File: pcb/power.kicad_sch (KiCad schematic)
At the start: 7 parts

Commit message: Changed resistor and cap footprints to CRGM
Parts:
- R12: footprint Resistor_SMD:R_0603_1608Metric -> CRGM Passive:R_0603_1608Metric
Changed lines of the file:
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@@
 			)
 		)
-		(property "Footprint" "Resistor_SMD:R_0603_1608Metric"
+		(property "Footprint" "CRGM Passive:R_0603_1608Metric"
 			(at 45.72 36.83 0)
 			(effects

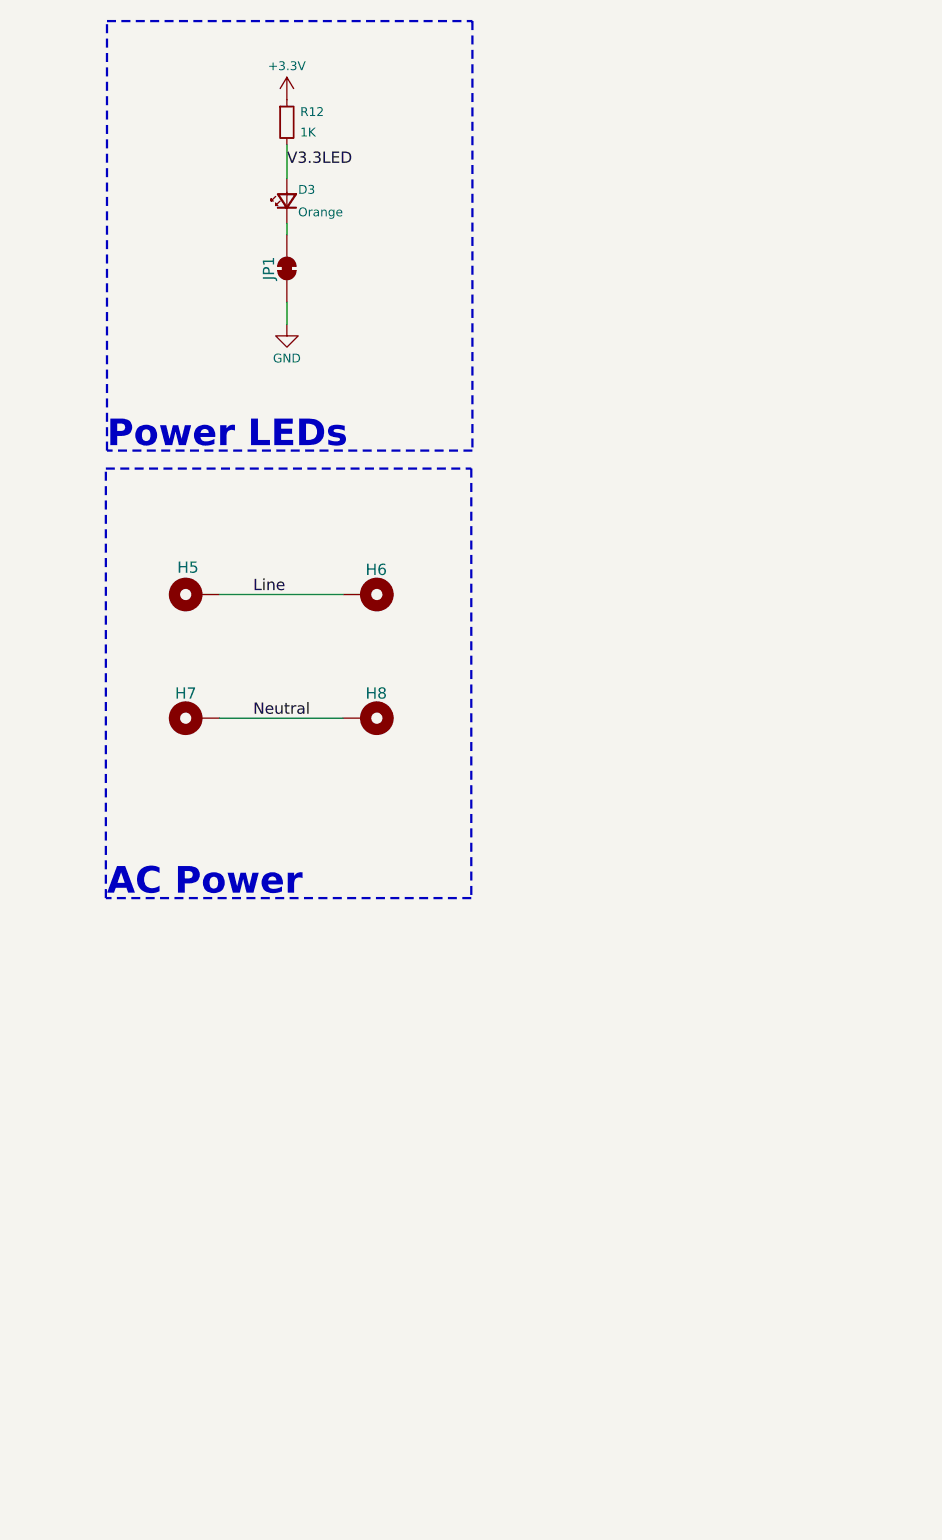
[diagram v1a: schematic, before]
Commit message: Removed CSV bom file; moved logos to symbols
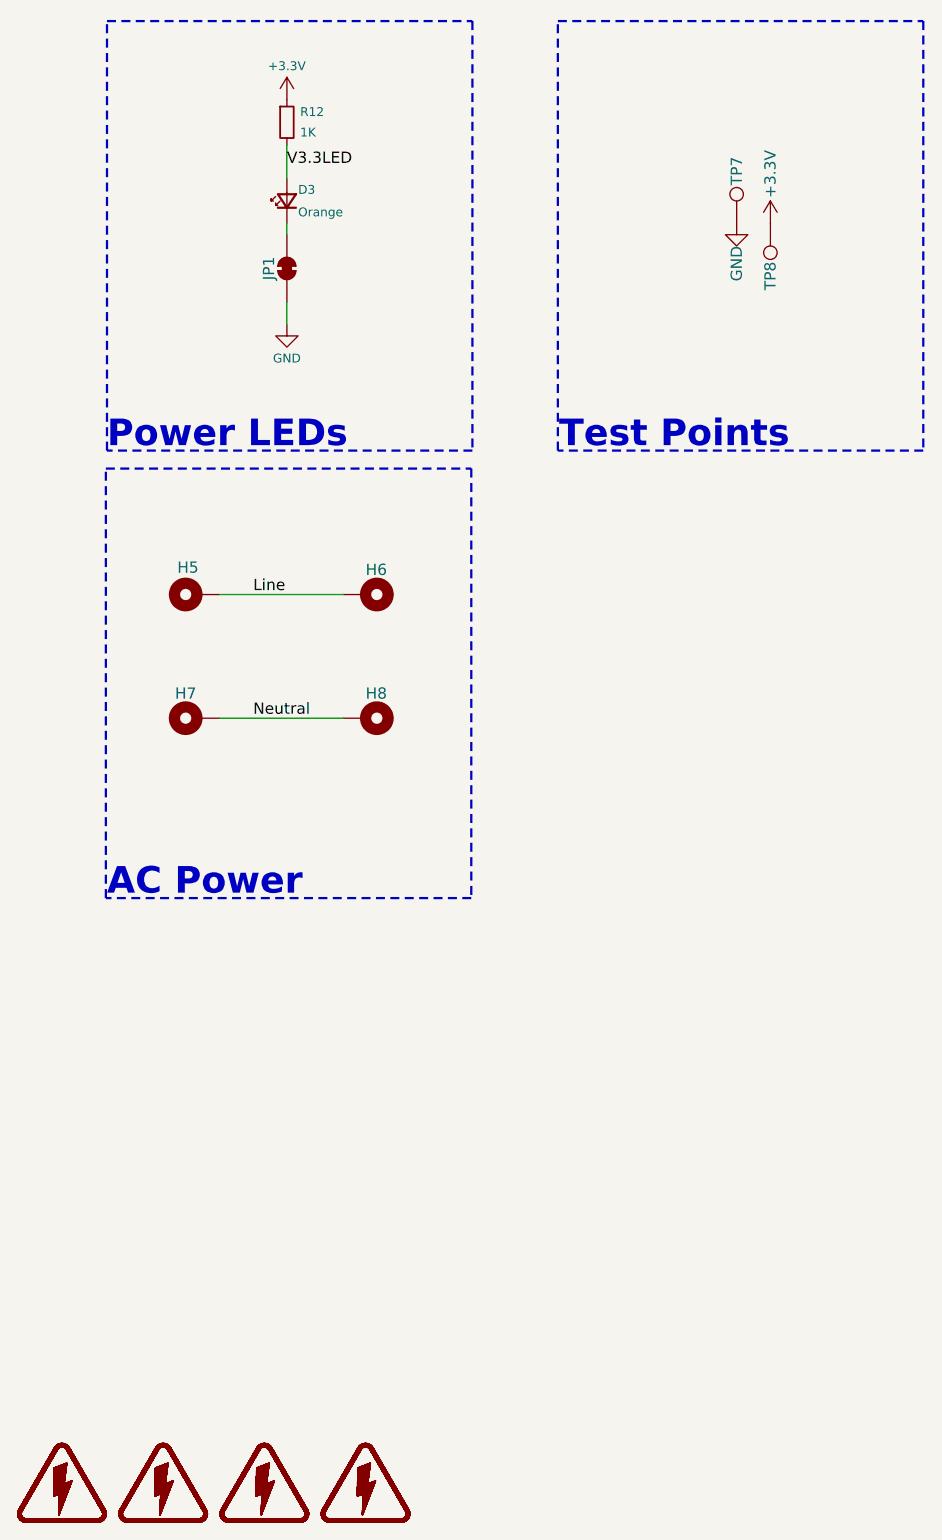
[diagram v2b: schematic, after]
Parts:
- added S1, S2, S3, S4: ~, CRGM Symbols:HIGH-VOLTAGE-5MM, symbol CRGM Symbols:High Voltage
- added TP7, TP8: ~, CRGM Mechanical:TestPoint_Pad_D1.0mm, symbol Connector:TestPoint
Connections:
- net +3.3V: now also TP8.1
- net GND: now also TP7.1
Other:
- note added: "Test Points"
- title: Current Detector -> Current Sensor

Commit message: Updated to all CRGM footprints
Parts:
- D3: footprint LED_SMD:LED_0603_1608Metric -> CRG Makes:LED_0603_1608Metric
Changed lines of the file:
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@@
 			)
 		)
-		(property "Footprint" "LED_SMD:LED_0603_1608Metric"
+		(property "Footprint" "CRG Makes:LED_0603_1608Metric"
 			(at 45.72 45.72 0)
 			(effects

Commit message: Updated part properties for consistency
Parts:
- R12: MN Vishay -> FOJAN; MPN CRCW06031K00FKEA -> FRC0603J102 TS; Tolerance (none) -> 5%
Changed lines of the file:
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@@
 			)
 		)
-		(property "MN" "Vishay"
+		(property "MN" "FOJAN"
 			(at 45.72 36.83 0)
 			(effects
@@
 			)
 		)
-		(property "MPN" "CRCW06031K00FKEA"
+		(property "MPN" "FRC0603J102 TS"
 			(at 45.72 36.83 0)
 			(effects
@@
 				)
 				(hide yes)
+			)
+		)
+		(property "Tolerance" "5%"
+			(at 45.72 36.83 0)
+			(effects
+				(font
+					(size 1.27 1.27)
+				)
+				(hide yes)

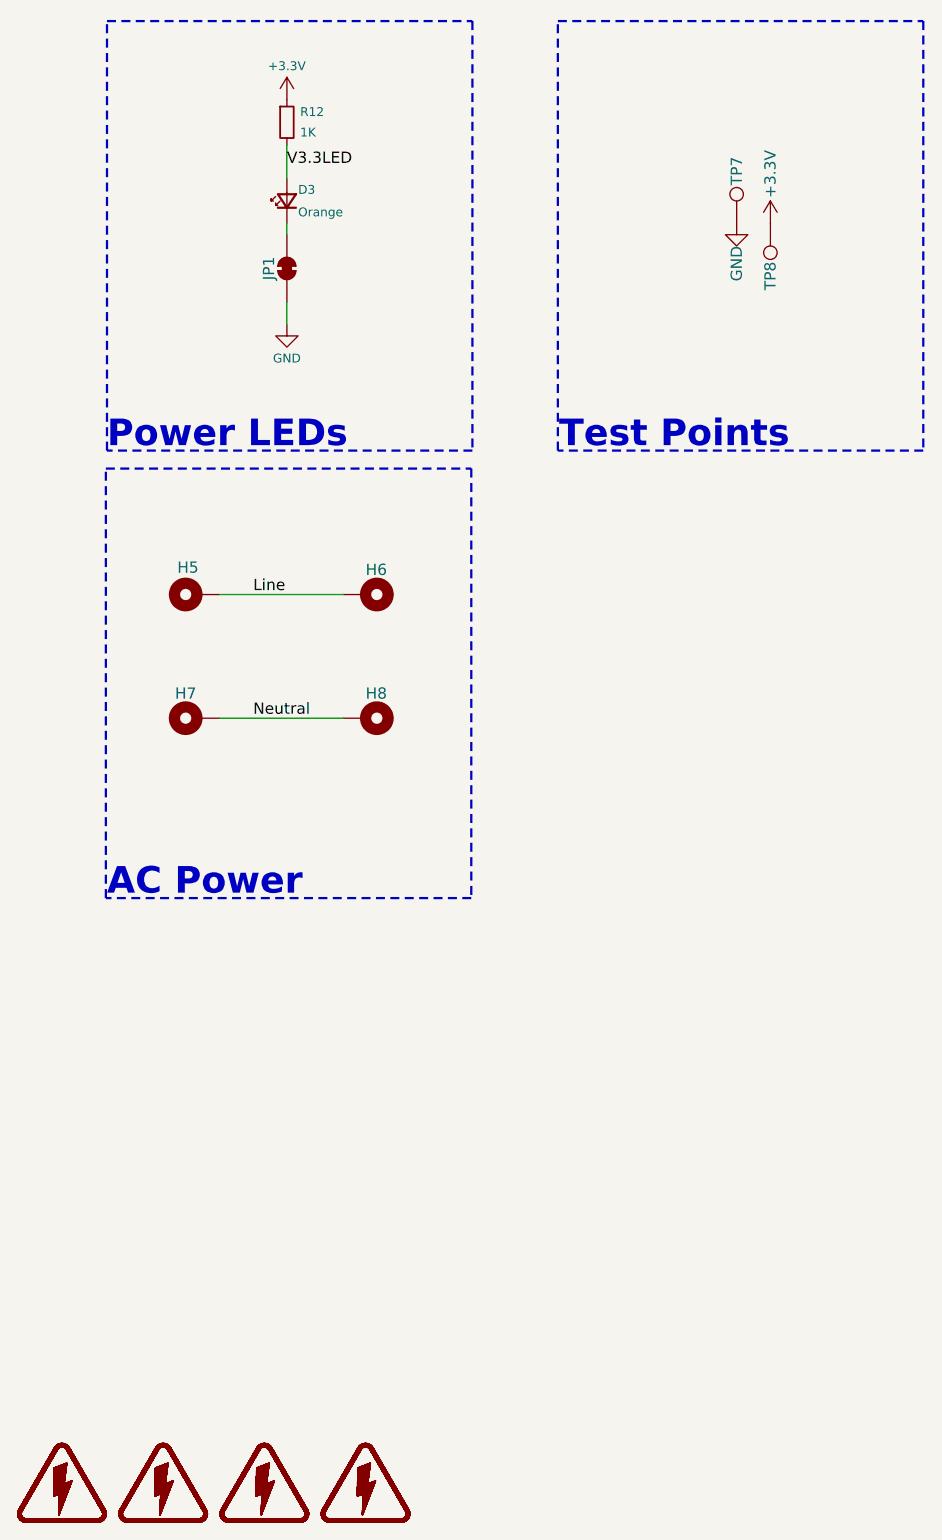
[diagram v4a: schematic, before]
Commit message: Fixed line thickness
Moved logos
Fixed board fillet to 3mm
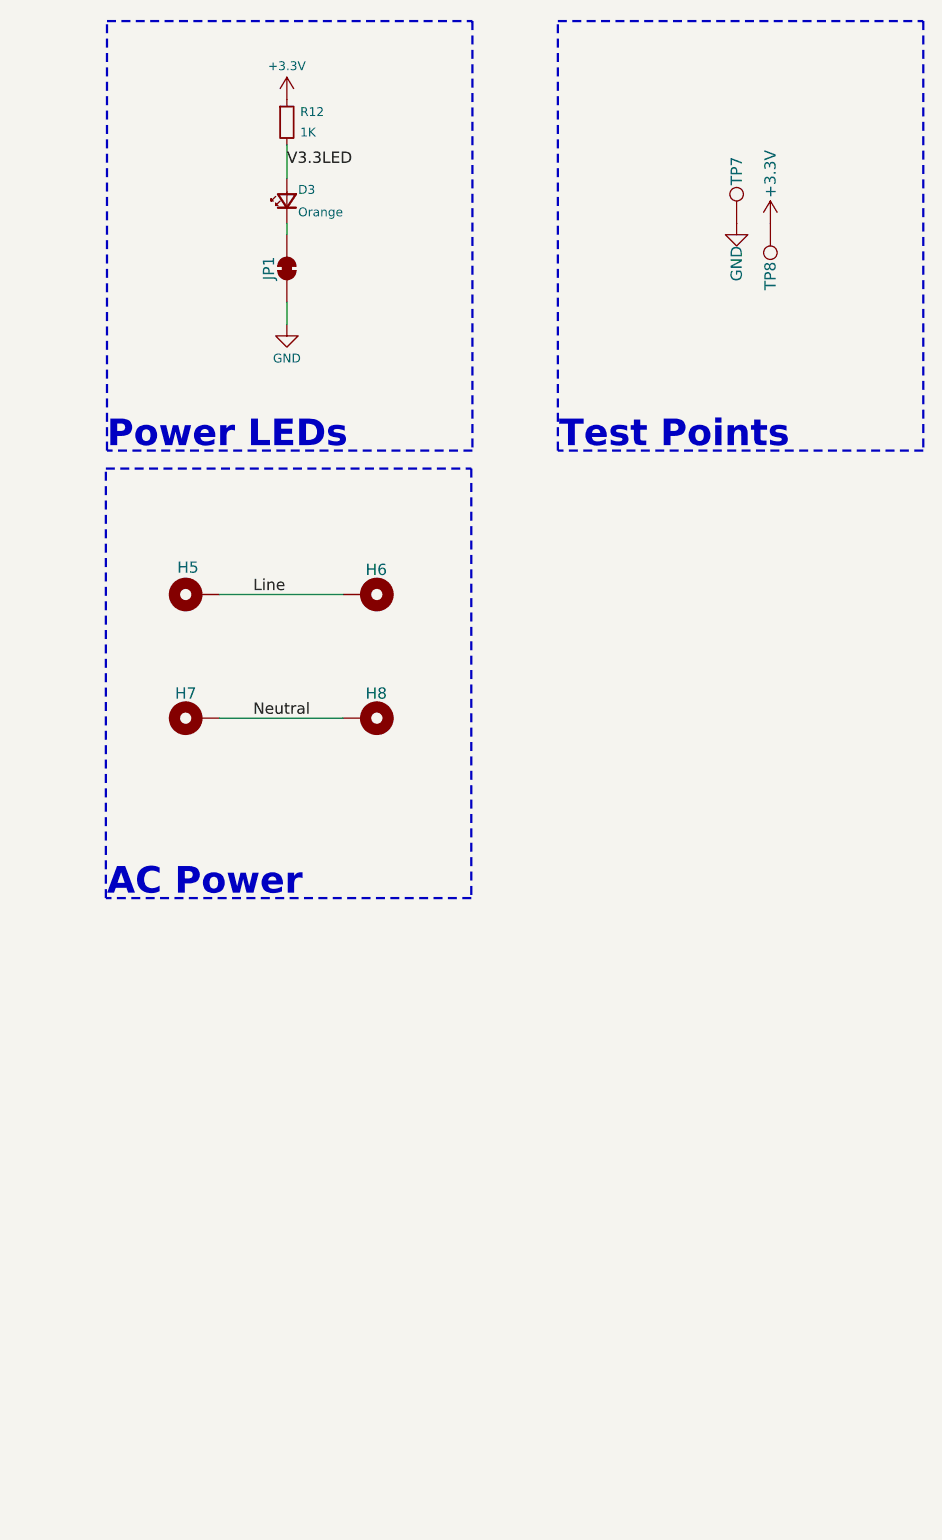
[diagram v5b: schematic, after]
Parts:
- removed S1, S2, S3, S4: ~, CRGM Symbols:HIGH-VOLTAGE-5MM, symbol CRGM Symbols:High Voltage

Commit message: Redesign with MCU
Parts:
- removed TP7, TP8: ~, CRGM Mechanical:TestPoint_Pad_D1.0mm, symbol Connector:TestPoint
- added D3: Orange, CRGM Passive:LED_0603_1608Metric, symbol Device:LED_Small
- added JP1: ~, CRGM Connector:SolderJumper-2_P1.3mm_Bridged_RoundedPad1.0x1.5mm, symbol Jumper:SolderJumper_2_Bridged
- added R15: 1K, CRGM Passive:R_0603_1608Metric, symbol Device:R_Small
- D5: renamed from D3; footprint CRG Makes:LED_0603_1608Metric -> CRGM Passive:LED_0603_1608Metric
- R12: value 1K -> 4.7K; Digikey 541-3991-2-ND -> 541-3993-2-ND; LCSC C2907113 -> C2907166; MPN FRC0603J102 TS -> FRC0603J472 TS; Mouser 71-CRCW06031K00JNEAC -> 71-CRCW06034K70JNEAC; Tolerance 5% -> (none)
- renumbered JP1 to JP6
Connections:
- net +3.3V: now also R15.1; no longer R12.1
- net GND: now also JP1.1 (A)
- net V3.3LED: now also R15.2; no longer R12.2
- new net: D3.1 (K), JP1.2 (B)
- new net +5V: R12.1
- new net V5LED: D3.2 (A), R12.2
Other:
- note removed: "Test Points"
- moved on the sheet: D5, H5, H6, H7, H8, JP6

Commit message: Fixed LCSC part numbers and attributes
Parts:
- R12: MN FOJAN -> FOJAN; Tolerance (none) -> 5%
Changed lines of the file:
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@@
 			)
 		)
-		(property "MN" "FOJAN"
+		(property "MN" "FOJAN "
 			(at 38.1 87.63 0)
 			(effects
@@
 				)
 				(hide yes)
+			)
+		)
+		(property "Tolerance" "5%"
+			(at 38.1 87.63 0)
+			(effects
+				(font
+					(size 1.27 1.27)
+				)
+				(hide yes)
